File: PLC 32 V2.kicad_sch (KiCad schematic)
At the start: 117 parts, among them J1 USB_C_Receptacle_USB2.0, J2 Screw_Terminal_01x05, J3 Screw_Terminal_01x05, J4 Screw_Terminal_01x02, J7 MODULO RTC, Q1 PMBT3904YS, Q2 FQP27P06, Q3 FQP27P06, Q4 FQP27P06, Q5 FQP27P06, Q6 FQP27P06, Q7 FQP27P06, Q8 BTA16-600C, Q9 BTA16-600C, SW1 SW_Push, SW2 SW_Push, U1 ILD74, U10 74HC14, U11 74HC14, U12 74HC14, U13 74HC14, U14 74HC14, U15 74HC14, U16 CH340C, U17 LM2576HVS-3.3, U18 ESP32-WROOM-32D, U2 ILD74, U21 ILD74, U22 ILD74, U23 ILD74, U24 ILD74, U25 ILD74, U26 ILD74, U27 MOC3021M, U28 MOC3021M, U29 ILD74, U3 ILD74, U30 74HC373, U4 ILD74, U5 ILD74, U6 ILD74, U7 ILD74, U8 74HC14, U9 74HC14

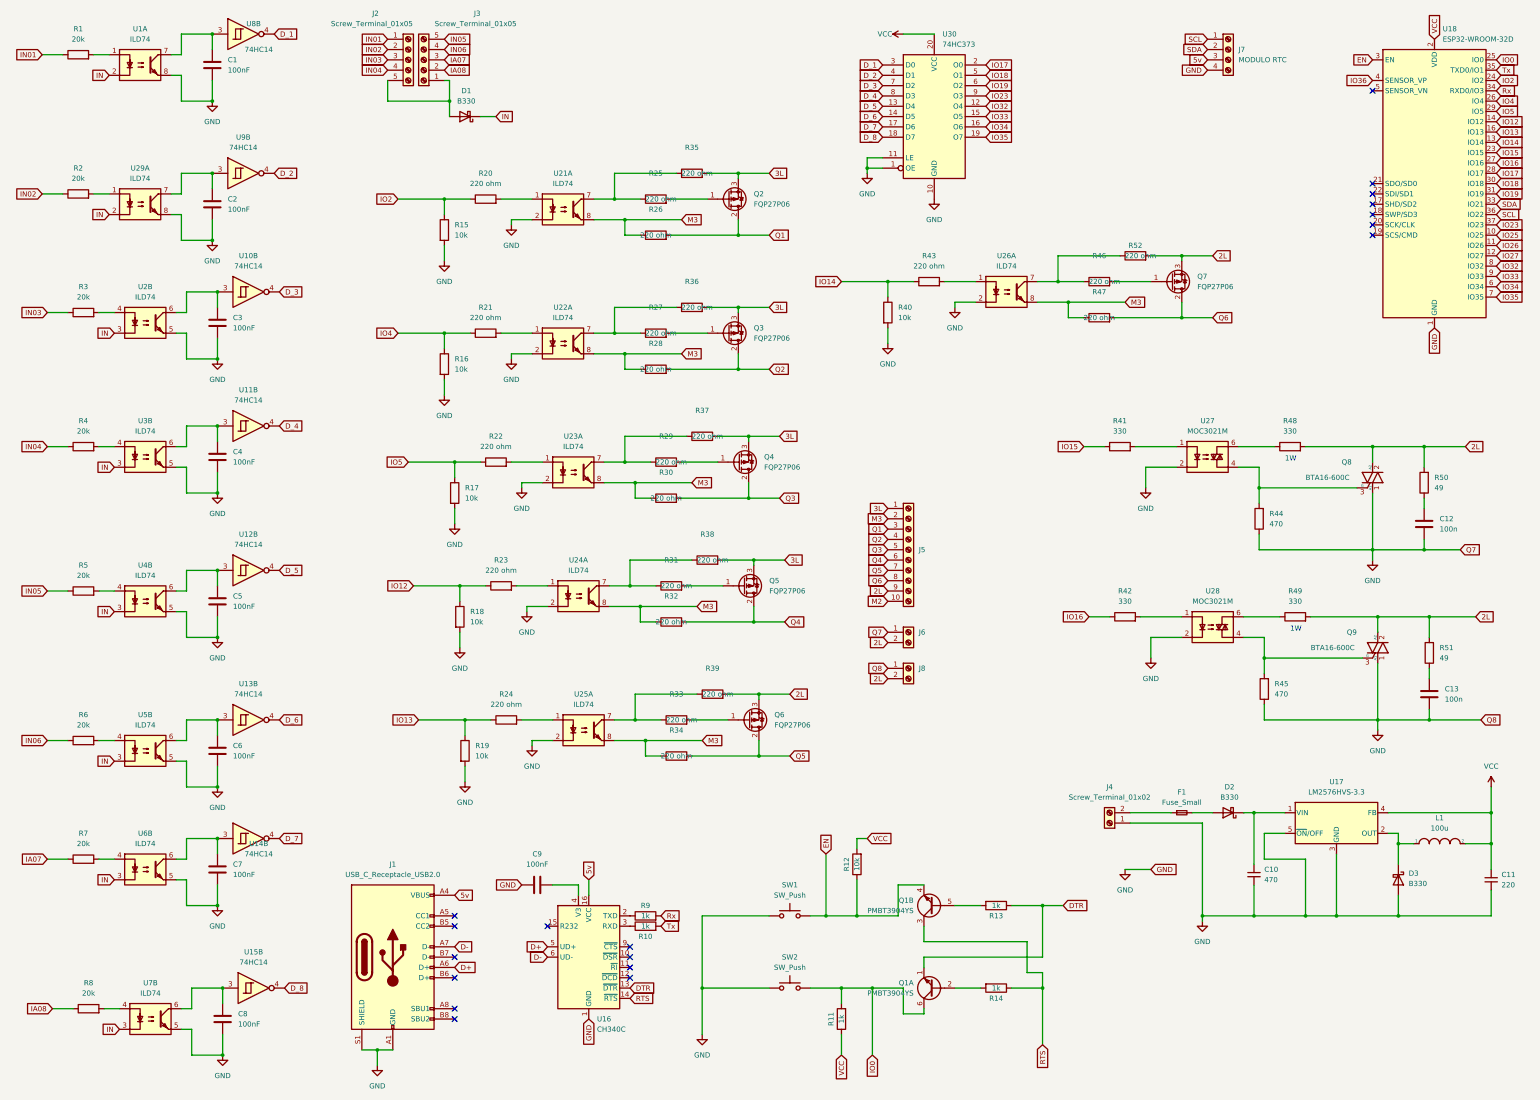
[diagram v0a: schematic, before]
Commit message: Diagrama por etapas
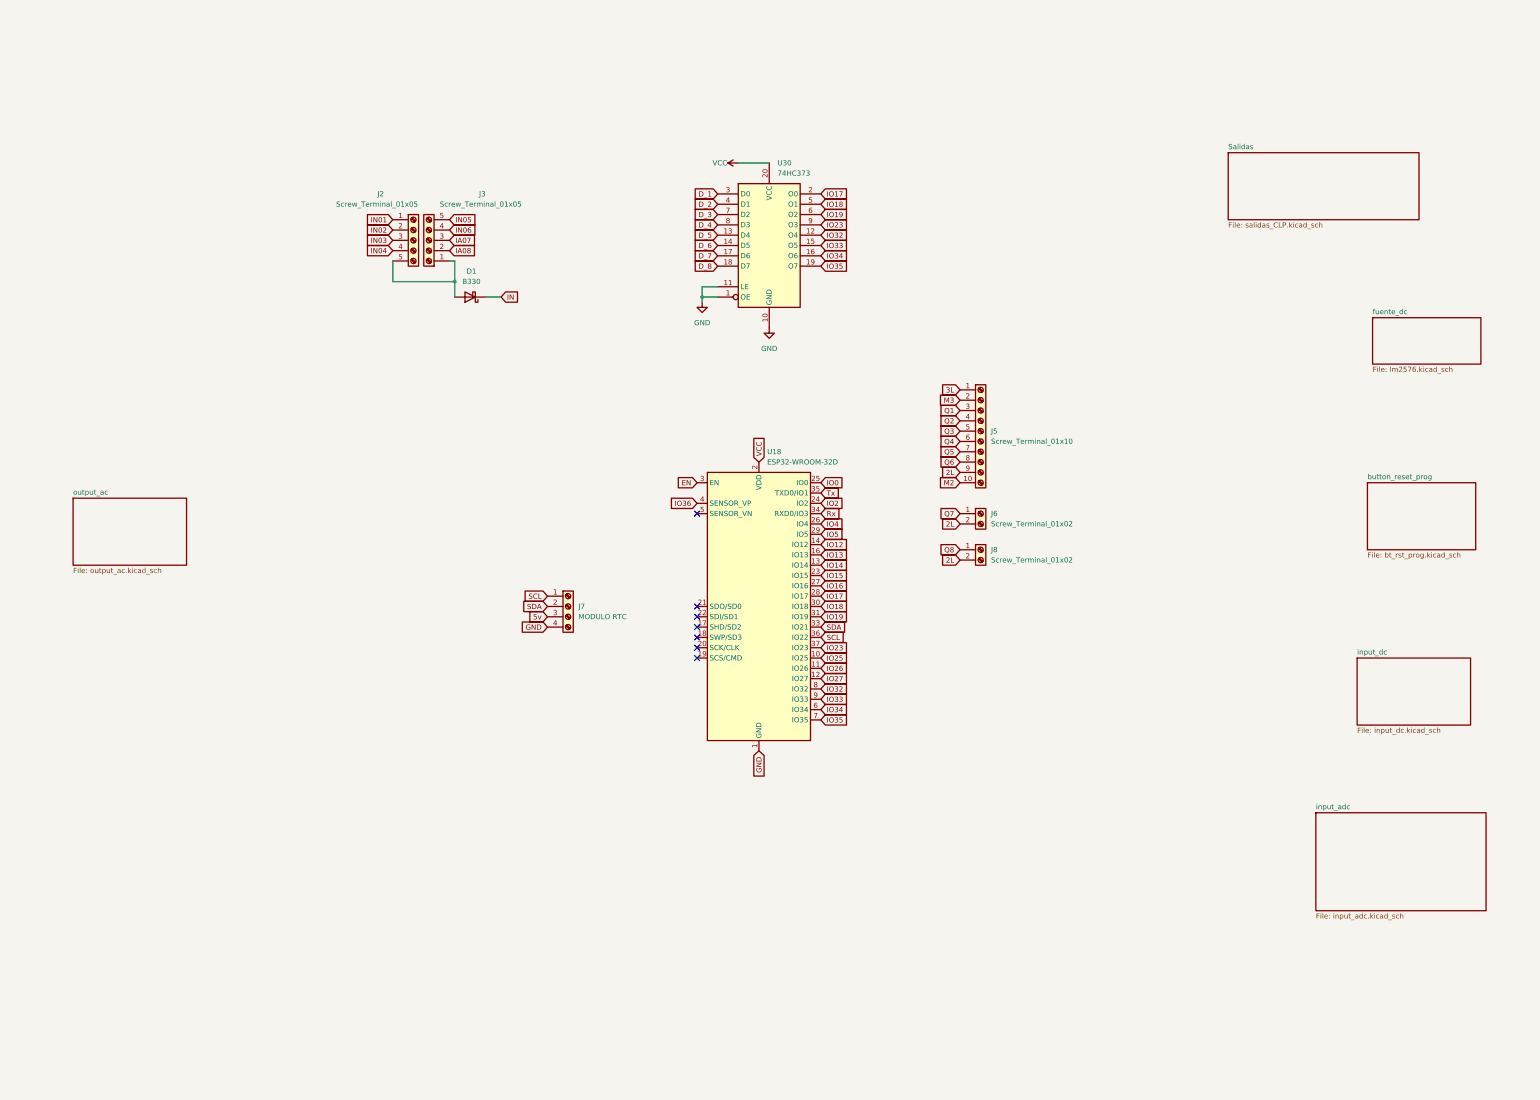
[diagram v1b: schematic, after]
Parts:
- removed C1, C2, C3, C4, C5, C6, C7, C8, C9: 100nF, Capacitor_SMD:C_0402_1005Metric, symbol Device:C
- removed C10: 470, Capacitor_SMD:C_Elec_10x10.2, symbol Device:C_Small
- removed C11: 220, Capacitor_SMD:C_Elec_6.3x7.7, symbol Device:C_Small
- removed C12, C13: 100n, Capacitor_THT:C_Rect_L31.5mm_W13.0mm_P27.50mm_MKS4, symbol Device:C
- removed D2, D3: B330, Diode_SMD:D_0402_1005Metric, symbol Diode:B330
- removed F1: Fuse_Small, Fuse:Fuse_0805_2012Metric, symbol Device:Fuse_Small
- removed J1: USB_C_Receptacle_USB2.0, Connector_USB:USB_C_Receptacle_HRO_TYPE-C-31-M-12, symbol Connector:USB_C_Receptacle_USB2.0
- removed J4: Screw_Terminal_01x02, TerminalBlock:TerminalBlock_bornier-2_P5.08mm, symbol Connector:Screw_Terminal_01x02
- removed L1: 100u, Inductor_SMD:L_TDK_SLF10165, symbol pspice:INDUCTOR
- removed Q1: PMBT3904YS, Package_TO_SOT_SMD:SOT-363_SC-70-6, symbol Transistor_BJT:PMBT3904YS
- removed Q2, Q3, Q4, Q5, Q6, Q7: FQP27P06, Package_TO_SOT_SMD:TO-252-2_TabPin1, symbol Transistor_FET:FQP27P06
- removed Q8, Q9: BTA16-600C, Package_TO_SOT_THT:TO-220-3_Vertical, symbol Triac_Thyristor:BTA16-600C
- removed R1, R2, R3, R4, R5, R6, R7, R8: 20k, Resistor_SMD:R_0603_1608Metric_Pad0.98x0.95mm_HandSolder, symbol Device:R
- removed R10, R11, R13, R14, R9: 1k, Resistor_SMD:R_0603_1608Metric_Pad0.98x0.95mm_HandSolder, symbol Device:R
- removed R12, R15, R16, R17, R18, R19, R40: 10k, Resistor_SMD:R_0603_1608Metric_Pad0.98x0.95mm_HandSolder, symbol Device:R
- removed R20, R21, R22, R23, R24, R25, R26, R27, R28, R29, R30, R31, R32, R33, R34, R35, R36, R37, R38, R39, R43, R46, R47: 220 ohm, Resistor_SMD:R_0603_1608Metric_Pad0.98x0.95mm_HandSolder, symbol Device:R
- removed R41, R42: 330, Resistor_SMD:R_0603_1608Metric_Pad0.98x0.95mm_HandSolder, symbol Device:R
- removed R44, R45: 470, Resistor_THT:R_Axial_DIN0414_L11.9mm_D4.5mm_P15.24mm_Horizontal, symbol Device:R
- removed R48, R49: 330, Resistor_THT:R_Axial_DIN0207_L6.3mm_D2.5mm_P7.62mm_Horizontal, symbol Device:R
- removed R50, R51: 49, Resistor_THT:R_Axial_DIN0414_L11.9mm_D4.5mm_P15.24mm_Horizontal, symbol Device:R
- removed R52: 220 ohm, Resistor_SMD:R_0612_1632Metric, symbol Device:R
- removed SW1, SW2: SW_Push, Button_Switch_SMD:SW_SPST_CK_RS282G05A3, symbol Switch:SW_Push
- removed U1, U2, U21, U22, U23, U24, U25, U26, U29, U3, U4, U5, U6, U7: ILD74, Package_DIP:DIP-4_W7.62mm, symbol Isolator:ILD74
- removed U10, U11, U12, U13, U14, U15, U8, U9: 74HC14, Package_SO:TSSOP-14_4.4x5mm_P0.65mm, symbol 74xx:74HC14
- removed U16: CH340C, Package_SO:SOIC-16_3.9x9.9mm_P1.27mm, symbol Interface_USB:CH340C
- removed U17: LM2576HVS-3.3, Package_TO_SOT_SMD:TO-263-5_TabPin3, symbol Regulator_Switching:LM2576HVS-3.3
- removed U27, U28: MOC3021M, Package_DIP:DIP-6_W7.62mm, symbol Relay_SolidState:MOC3021M
- J5: value (none) -> Screw_Terminal_01x10; footprint (none) -> TerminalBlock_Phoenix:TerminalBlock_Phoenix_PT-1,5-10-5.0-H_1x10_P5.00mm_Horizontal
- J6, J8: value (none) -> Screw_Terminal_01x02; footprint (none) -> TerminalBlock:TerminalBlock_bornier-2_P5.08mm
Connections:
- net GND: no longer J6.1 (Pin_1), J8.1 (Pin_1)
- new net Q7: J6.1 (Pin_1)
- new net Q8: J8.1 (Pin_1)
- no-connect marks 18 -> 7
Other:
- added sheet Salidas (salidas_CLP.kicad_sch)
- added sheet button_reset_prog (bt_rst_prog.kicad_sch)
- added sheet fuente_dc (lm2576.kicad_sch)
- added sheet input_adc (input_adc.kicad_sch)
- added sheet input_dc (input_dc.kicad_sch)
- added sheet output_ac (output_ac.kicad_sch)
- note removed: "1W"
- moved on the sheet: D1, J2, J3, J5, J6, J7, J8, U18, U30

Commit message: Esquema con comentarios
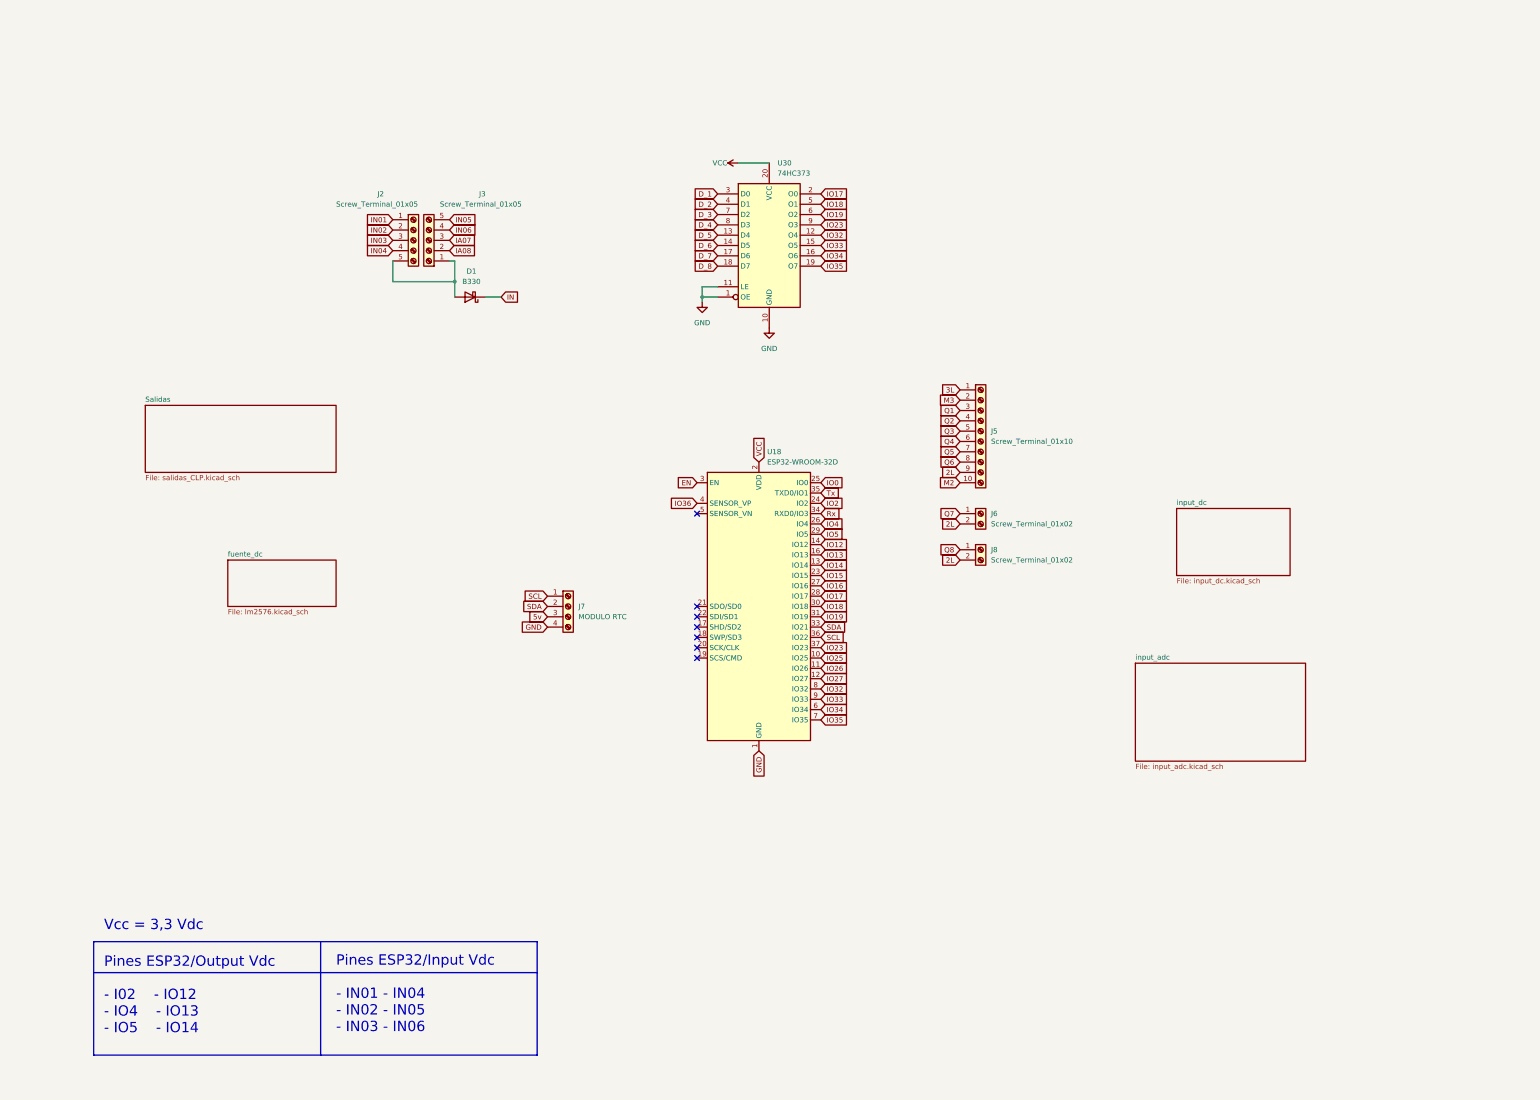
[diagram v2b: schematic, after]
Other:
- removed sheet button_reset_prog
- removed sheet output_ac
- note added: "Pines ESP32/Input Vdc - IN01 - IN04 - IN02 - IN05 - IN03 - IN06"
- note added: "Pines ESP32/Output Vdc - I02 - IO12 - IO4 - IO13 - IO5 - IO14"
- note added: "Vcc = 3,3 Vdc"

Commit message: Init Documentación
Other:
- sheet Salidas renamed Salidas_DC
- sheet fuente_dc renamed Fuente_DC-DC
- sheet input_adc renamed Input_ADC
- sheet input_dc renamed Input_DC
- note added: "Pines ESP32/Input ADC - IA07 - IA08"
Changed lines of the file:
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@@
   )
   (polyline (pts (xy 96.52 243.84) (xy 96.52 271.78))
-    (stroke (width 0) (type default) (color 0 0 0 0))
-  )
-  (polyline (pts (xy 40.64 251.46) (xy 149.86 251.46))
-    (stroke (width 0) (type default) (color 0 0 0 0))
+    (stroke (width 0) (type solid) (color 30 0 0 1))
+  )
+  (polyline (pts (xy 40.64 251.46) (xy 203.2 251.46))
+    (stroke (width 0) (type dash) (color 30 0 0 1))
   )
   (polyline (pts (xy 40.64 243.84) (xy 40.64 271.78))
-    (stroke (width 0) (type default) (color 0 0 0 0))
+    (stroke (width 0) (type solid) (color 8 0 0 1))
   )
   (wire (pts (xy 114.3 81.28) (xy 129.54 81.28))
@@
   )
   (polyline (pts (xy 149.86 243.84) (xy 149.86 271.78))
-    (stroke (width 0) (type default) (color 0 0 0 0))
+    (stroke (width 0) (type solid) (color 8 0 0 1))
   )
   (wire (pts (xy 199.39 52.07) (xy 207.01 52.07))
@@
   )
   (polyline (pts (xy 40.64 271.78) (xy 96.52 271.78))
-    (stroke (width 0) (type default) (color 0 0 0 0))
+    (stroke (width 0) (type solid) (color 8 0 0 1))
   )
   (wire (pts (xy 190.5 82.55) (xy 190.5 85.09))
     (stroke (width 0) (type default) (color 0 0 0 0))
   )
+  (polyline (pts (xy 149.86 243.84) (xy 203.2 243.84))
+    (stroke (width 0) (type solid) (color 30 0 0 1))
+  )
+  (polyline (pts (xy 203.2 271.78) (xy 149.86 271.78))
+    (stroke (width 0) (type solid) (color 8 0 0 1))
+  )
   (polyline (pts (xy 149.86 271.78) (xy 96.52 271.78))
-    (stroke (width 0) (type default) (color 0 0 0 0))
+    (stroke (width 0) (type solid) (color 8 0 0 1))
   )
   (polyline (pts (xy 40.64 243.84) (xy 149.86 243.84))
-    (stroke (width 0) (type default) (color 0 0 0 0))
+    (stroke (width 0) (type solid) (color 30 0 0 1))
   )
   (wire (pts (xy 194.31 85.09) (xy 190.5 85.09))
     (stroke (width 0) (type default) (color 0 0 0 0))
   )
+  (polyline (pts (xy 203.2 243.84) (xy 203.2 271.78))
+    (stroke (width 0) (type solid) (color 8 0 0 1))
+  )
   (text "Pines ESP32/Input Vdc\n\n- IN01 - IN04\n- IN02 - IN05\n- IN03 - IN06\n\n"
-    (at 100.33 270.51 0)
+    (at 100.33 269.875 0)
     (effects (font (size 2.54 2.54)) (justify left bottom))
   )
@@
   )
   (text "Pines ESP32/Output Vdc\n\n- I02	- IO12\n- IO4	- IO13\n- IO5	- IO14"
-    (at 43.18 266.7 0)
+    (at 43.18 266.065 0)
+    (effects (font (size 2.54 2.54)) (justify left bottom))
+  )
+  (text "Pines ESP32/Input ADC\n\n- IA07\n- IA08\n\n\n" (at 156.21 269.875 0)
     (effects (font (size 2.54 2.54)) (justify left bottom))
   )
@@
     (stroke (width 0.1524) (type solid) (color 0 0 0 0))
     (fill (color 0 0 0 0.0000))
-    (property "Sheet name" "input_adc" (id 0) (at 297.18 174.5484 0)
-      (effects (font (size 1.27 1.27)) (justify left bottom))
+    (property "Sheet name" "Input_ADC" (id 0) (at 297.18 173.9134 0)
+      (effects (font (size 2.54 2.54)) (justify left bottom))
     )
     (property "Sheet file" "input_adc.kicad_sch" (id 1) (at 297.18 199.9746 0)
@@
     (stroke (width 0.1524) (type solid) (color 0 0 0 0))
     (fill (color 0 0 0 0.0000))
-    (property "Sheet name" "fuente_dc" (id 0) (at 73.66 149.1484 0)
-      (effects (font (size 1.27 1.27)) (justify left bottom))
+    (property "Sheet name" "Fuente_DC-DC" (id 0) (at 73.66 148.5134 0)
+      (effects (font (size 2.54 2.54)) (justify left bottom))
     )
     (property "Sheet file" "lm2576.kicad_sch" (id 1) (at 73.66 161.8746 0)
@@
     (stroke (width 0.1524) (type solid) (color 0 0 0 0))
     (fill (color 0 0 0 0.0000))
-    (property "Sheet name" "input_dc" (id 0) (at 307.34 136.4484 0)
-      (effects (font (size 1.27 1.27)) (justify left bottom))
+    (property "Sheet name" "Input_DC" (id 0) (at 307.34 135.8134 0)
+      (effects (font (size 2.54 2.54)) (justify left bottom))
     )
     (property "Sheet file" "input_dc.kicad_sch" (id 1) (at 307.34 154.2546 0)
@@
     (stroke (width 0.1524) (type solid) (color 0 0 0 0))
     (fill (color 0 0 0 0.0000))
-    (property "Sheet name" "Salidas" (id 0) (at 53.34 111.0484 0)
-      (effects (font (size 1.27 1.27)) (justify left bottom))
+    (property "Sheet name" "Salidas_DC" (id 0) (at 53.34 110.4134 0)
+      (effects (font (size 2.54 2.54)) (justify left bottom))
     )
     (property "Sheet file" "salidas_CLP.kicad_sch" (id 1) (at 53.34 128.8546 0)
